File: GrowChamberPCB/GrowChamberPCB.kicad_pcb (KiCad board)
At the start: 2 copper layers, 100 x 100 mm, 194 parts, among them J1 Mister, J10 FoggerBasin, J11 TP, J12 Moisture Sensor 3, J13 Moisture Sensor 2, J14 UART, J15 FAE Fan, J16 DrainLevel, J17 TP, J18 TP, J19 TP, J2 Moisture Sensor 1, J20 TP, J21 TP, J22 TP, J23 TP, J24 TP, J25 TP, J26 TP, J27 TP, J28 TP, J29 TP, J3 SCD30, J30 TP, J31 TP, J32 TP, J33 TP, J34 TP, J35 TP, J36 TP, J37 TP, J38 TP, J39 TP, J4 Heater Fans, J40 TP, J41 TP, J42 TP, J43 TP, J44 TP, J45 TP, J47 Conn_01x04, J48 Conn_01x09, J49 TP, J5 Fogger Solenoid, J50 TP, J51 TP, J52 TP, J53 TP, J6 Drain Solenoid, J7 Water Solenoid, J8 Glycol Solenoid, J9 CircFan, P1 12V_In, P2 120V, P3 Screw Terminal, Q1 MOSFET, Q10 NPN, Q11 MOSFET, Q12 NPN, Q13 MOSFET, Q15 NPN, Q17 NPN, Q18 MOSFET, Q2 NPN, Q3 MOSFET, Q4 NPN, Q5 MOSFET, Q6 NPN, Q7 MOSFET, Q8 BRT30N70P3, Q9 NPN, SW1 Reset_Button_Internal, SW2 ResetButton_External, SW3 Bootmode_Internal, SW4 BootMode_External, U10 1N4007W, U11 AP63203WU-7, U12 1N4007W, U13 1N4007W, U14 1N4007W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

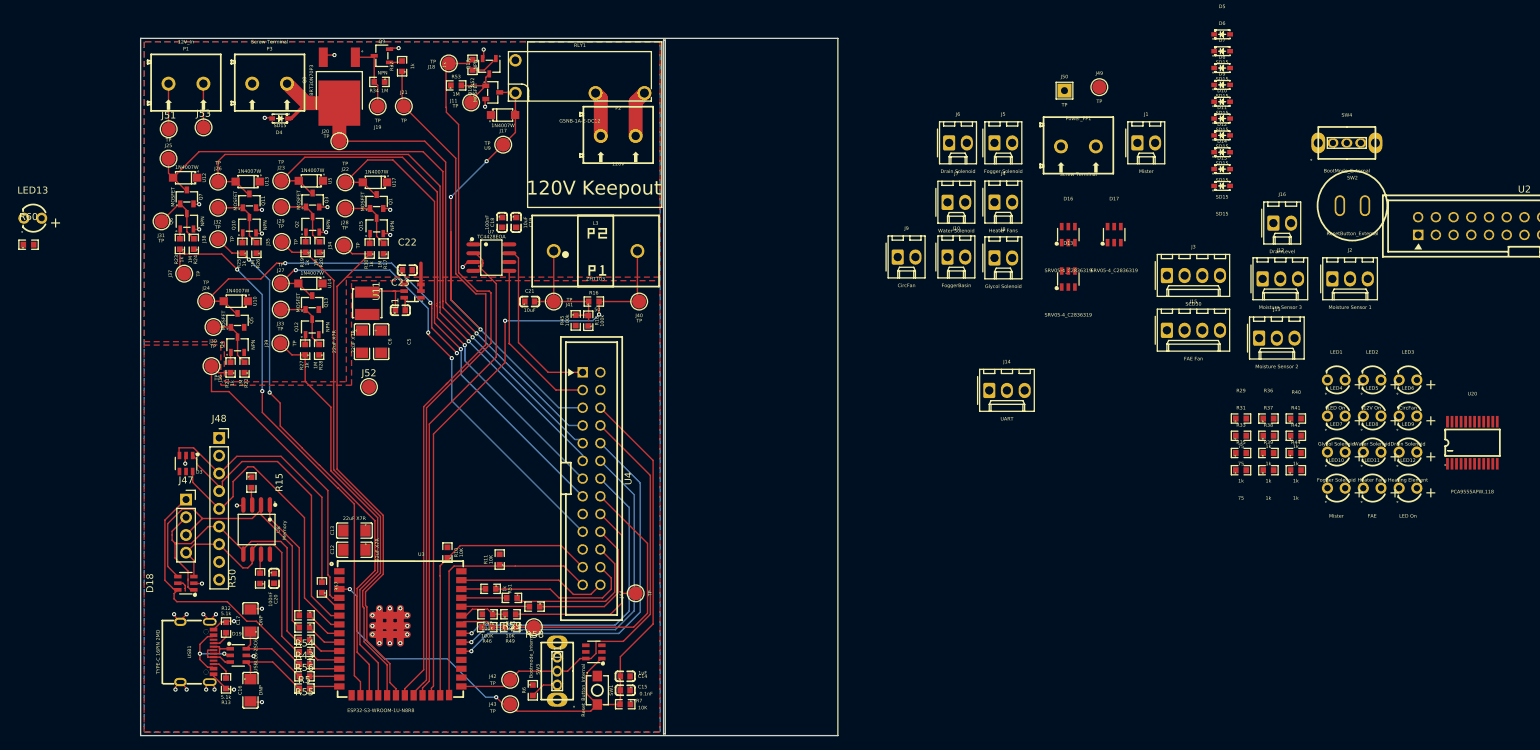
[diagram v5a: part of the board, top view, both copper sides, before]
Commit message: made a 4 layer board instead of 2
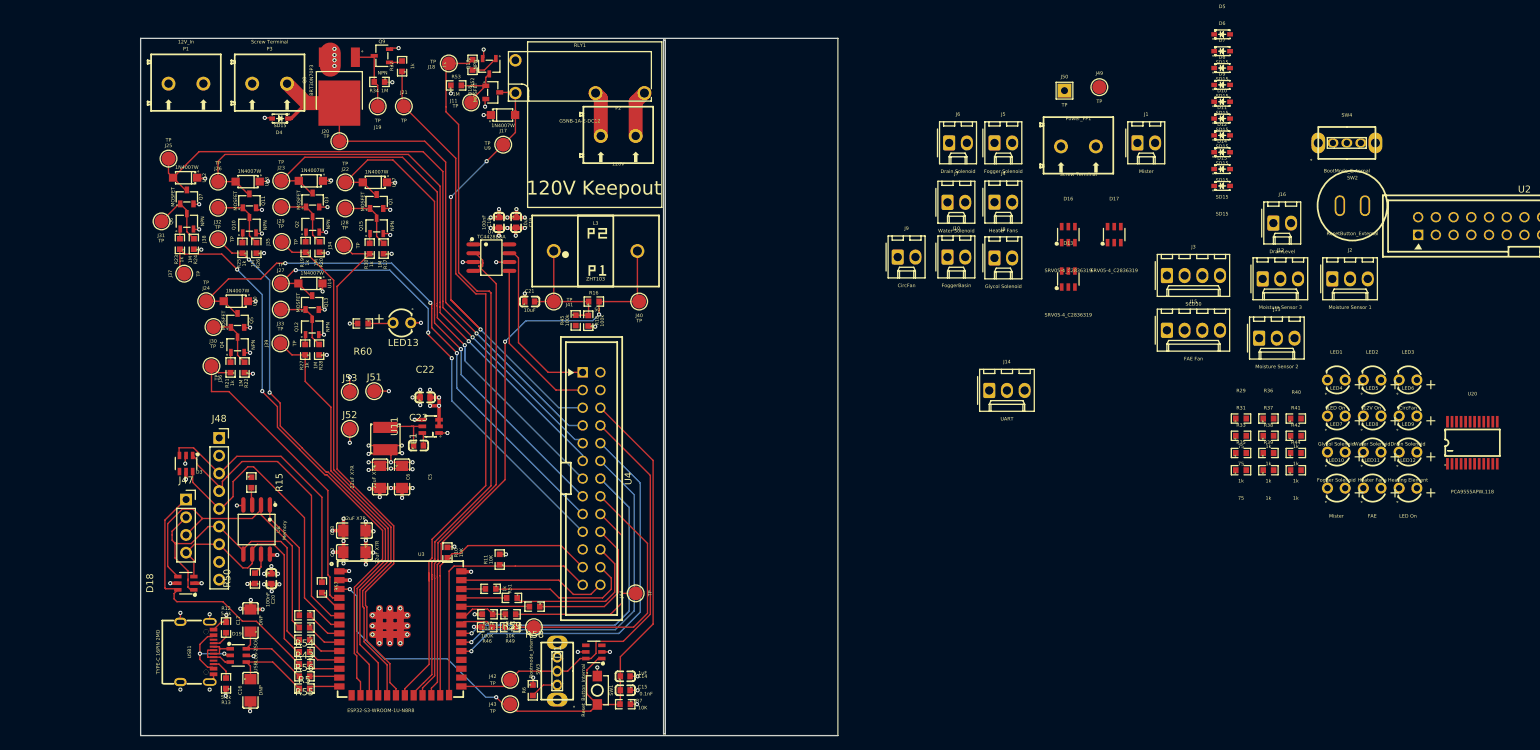
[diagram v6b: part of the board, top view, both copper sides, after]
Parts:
- moved LED13 55.0 mm to (49.5, 52.8), turned to 180 degrees
- moved R60 49.3 mm to (43.9, 52.9), turned to 180 degrees
- moved J51 47.8 mm to (45.5, 62.6)
- moved J53 43.3 mm to (42.0, 62.7)
- moved C5 19.6 mm to (49.5, 74.9)
- moved C23 19.6 mm to (51.9, 70.4)
- moved C6 19.6 mm to (46.4, 74.9)
- moved L1 19.6 mm to (47.1, 69.4)
- moved U11 19.6 mm to (53.6, 67.7)
- moved C22 18.4 mm to (52.8, 63.5)
- moved J52 6.60 mm to (42.0, 68.0)
- moved R50 0.74 mm to (28.4, 89.4)
- moved C18 0.45 mm to (63.4, 38.4)
- moved C20 0.39 mm to (30.8, 89.5)
- moved C12 0.35 mm to (42.7, 85.7)
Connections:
- LED13 pad 1: GND_FP -> GND
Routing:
- net 3.3V: track 1.99 -> 49.9 mm, vias 0 -> 31
- net 12V: track 10.5 -> 44.0 mm, vias 0 -> 27
- net GND: track 79.5 -> 110.6 mm, vias 42 -> 80
- net DrainSol: track 50.9 -> 81.4 mm
- net Heater_ON: track 77.0 -> 67.2 mm
- net Net-(LED13-A): track 0.00 -> 3.62 mm
- net WaterSol_IO: track 81.6 -> 85.1 mm
- net KSD_Fault: track 86.9 -> 85.2 mm
- net GlycolSol_IO: track 77.4 -> 78.8 mm
- net HeaterFans_IO: track 75.2 -> 76.5 mm
- net CircFan_IO: track 59.5 -> 60.7 mm
- net FoggerSol_IO: track 74.6 -> 75.8 mm
- net Net-(J41-Pin_1): track 19.6 -> 18.8 mm
- net CS_SD: track 39.2 -> 39.8 mm
- added copper zone on In2.Cu, net 12V
- added copper zone on In2.Cu, net 3.3V
- added copper zone on In1.Cu, net GND
- removed copper zone on F.Cu, net 12V
- removed copper zone on F.Cu, net 3.3V
- removed copper zone on B.Cu, net GND
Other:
- copper layers 2 -> 4
- rule pad_to_mask_clearance: 0 -> 0.1

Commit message: fillin stuff out
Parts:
- moved U2 105.4 mm to (105.1, 34.6), turned to 90 degrees
- moved J2 95.5 mm to (92.3, 16.4)
- moved SW2 95.1 mm to (93.6, 59.2)
- moved SW4 93.6 mm to (94.2, 49.6)
- moved J16 87.9 mm to (92.4, 70.0)
- moved Power_FP1 87.9 mm to (105.8, 105.4)
- moved J13 85.7 mm to (92.3, 24.8)
- moved J12 81.7 mm to (92.3, 33.4)
- moved J1 80.6 mm to (92.5, 78.0)
- moved J5 73.0 mm to (92.9, 87.0)
- moved J3 68.7 mm to (90.6, 42.2)
- moved J6 66.4 mm to (100.0, 87.2)
- moved J15 64.4 mm to (99.5, 78.0)
- moved J7 63.2 mm to (106.8, 95.2)
- moved J8 62.1 mm to (100.0, 95.2)
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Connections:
- J12 pad 3: GPIO4_FP -> SoilMoisture4_FP
- J13 pad 3: GPIO2_FP -> SoilMoisture2_FP
- J2 pad 3: GPIO1_FP -> SoilMoisture1_FP
- U2 pad 1: unconnected-(U2-Pad1) -> Piezo2_FP
- U2 pad 10: unconnected-(U2-Pad10) -> SoilMoisture4_FP
- U2 pad 11: unconnected-(U2-Pad11) -> GlycolSol_FP
- U2 pad 12: unconnected-(U2-Pad12) -> SoilMoisture2_FP
- U2 pad 13: unconnected-(U2-Pad13) -> FoggerSol_FP
- U2 pad 14: unconnected-(U2-Pad14) -> SoilMoisture1_FP
- U2 pad 15: unconnected-(U2-Pad15) -> Heater Fans_FP
- U2 pad 16: unconnected-(U2-Pad16) -> Drain_Level_FP
- U2 pad 17: unconnected-(U2-Pad17) -> DrainSol_FP
- U2 pad 18: unconnected-(U2-Pad18) -> Fogger_Basin_Float_Switch_FP
- U2 pad 19: unconnected-(U2-Pad19) -> Circ_Fan_FP
- U2 pad 2: unconnected-(U2-Pad2) -> 3.3V_FP
- U2 pad 20: unconnected-(U2-Pad20) -> RXD0_FP
- U2 pad 22: unconnected-(U2-Pad22) -> TXD0_FP
- U2 pad 23: unconnected-(U2-Pad23) -> SDA_FP
- U2 pad 24: unconnected-(U2-Pad24) -> External_Fan_PWM_FP
- U2 pad 25: unconnected-(U2-Pad25) -> SCL_FP
- U2 pad 26: unconnected-(U2-Pad26) -> Fan_Tach_FP
- U2 pad 3: unconnected-(U2-Pad3) -> Piezo1_FP
- U2 pad 4: unconnected-(U2-Pad4) -> 3.3V_FP
- U2 pad 5: unconnected-(U2-Pad5) -> Heater_ON_FP
- U2 pad 6: unconnected-(U2-Pad6) -> EN_FP
- U2 pad 7: unconnected-(U2-Pad7) -> LEDs_FP
- U2 pad 8: unconnected-(U2-Pad8) -> BootMode_FP
- U2 pad 9: unconnected-(U2-Pad9) -> WaterSol_FP
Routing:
- net GND: track 110.6 -> 112.3 mm, vias 80 -> 81
- net KSD_Fault: track 85.2 -> 86.4 mm
- net 3.3V: track 49.9 -> 50.8 mm, vias 31 -> 32
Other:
- outline, holes or cut-outs redrawn

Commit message: finished routing
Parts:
- removed C18, C23: 100nF, easyeda2kicad:C0603
- removed C19, C21, C22: 10uF, easyeda2kicad:C0603
- removed D13, D16, D17, D18: SRV05-4_C2836319, easyeda2kicad:SOT-23-6_L2.9-W1.6-P0.95-LS2.8-BL
- removed D14, D15: SD15, easyeda2kicad:SOD-323_L1.7-W1.3-LS2.6-RD
- removed D19: USBLC6-2SC6, easyeda2kicad:SOT-23-6_L2.9-W1.6-P0.95-LS2.8-BL
- removed J11, J17, J18, J19, J20, J21, J22, J23, J24, J25, J26, J27, J28, J29, J30, J31, J32, J33: TP, TestPoint:TestPoint_Pad_D2.0mm
- removed L1: ANR4030T3R9M, easyeda2kicad:IND-SMD_L4.0-W4.0
- removed LED11: FAE, easyeda2kicad:LED-TH_BD3.9-P2.54-RD_RED
- removed LED12: LED On, easyeda2kicad:LED-TH_BD3.9-P2.54-RD_RED
- removed Q1, Q18, Q3, Q5: MOSFET, easyeda2kicad:SOT-23-3_L2.9-W1.3-P1.90-LS2.4-BR
- removed Q17, Q2, Q4, Q6, Q9: NPN, easyeda2kicad:SOT-23-3_L3.0-W1.7-P0.95-LS2.9-BR
- removed Q8: BRT30N70P3, easyeda2kicad:TO-252-2_L6.6-W6.1-P4.60-LS10.0-BR-CW
- removed R40, R41, R42, R44, R51, R52: 1k, easyeda2kicad:R0603
- removed R48, R49, R50: 10K, easyeda2kicad:R0603
- removed R53: 1M, easyeda2kicad:R0603
- removed R54, R55, R56, R57, R58, R59: 33, easyeda2kicad:R0603
- removed SW2: ResetButton_External, easyeda2kicad:CONN-TH_PB-05B-R
- removed U10, U5, U9: 1N4007W, easyeda2kicad:SOD-123FL_L2.7-W1.8-LS3.7-RD
- removed U20: PCA9555APW,118, easyeda2kicad:TSSOP-24_L7.8-W4.4-P0.65-LS6.4-BL
- added C1: 4.7uF - X7R, easyeda2kicad:C1206, F.Cu at (106.8, 80.3)
- added C10: 22uF - X5R, easyeda2kicad:C1206, F.Cu at (93.6, 108.9)
- added C11: 47uF X5R, easyeda2kicad:C1206, F.Cu at (100.3, 92.7)
- added C2: 10nF, easyeda2kicad:C0603, F.Cu at (102.7, 85.2)
- added C3: 47uF X5R, easyeda2kicad:C1206, F.Cu at (95.1, 92.7)
- added C4: 100nF, easyeda2kicad:C0402, F.Cu at (102.9, 90.9)
- added C7: 150pF, easyeda2kicad:C0603, F.Cu at (108.8, 91.3)
- added C8: 1500pF, easyeda2kicad:C0603, F.Cu at (104.7, 91.2)
- added C9: 47uF X5R, easyeda2kicad:C1206, F.Cu at (97.7, 92.7)
- added D2: SS34, easyeda2kicad:SMA_L4.3-W2.6-LS5.2-RD, F.Cu at (100.4, 79.5)
- added D20: 1N4007W, easyeda2kicad:SOD-123FL_L2.7-W1.8-LS3.8-RD, F.Cu at (106.0, 61.8)
- added D27: 1n4007W, easyeda2kicad:SOD-123FL_L2.7-W1.8-LS3.8-RD, F.Cu at (82.4, 64.5)
- added D28: 1n4007W, easyeda2kicad:SOD-123FL_L2.7-W1.8-LS3.8-RD, F.Cu at (82.4, 51.8)
- added D29: 1n4007W, easyeda2kicad:SOD-123FL_L2.7-W1.8-LS3.8-RD, F.Cu at (73.6, 60.4)
- added D30: 1n4007W, easyeda2kicad:SOD-123FL_L2.7-W1.8-LS3.8-RD, F.Cu at (73.6, 73.1)
- added D31: 1n4007W, easyeda2kicad:SOD-123FL_L2.7-W1.8-LS3.8-RD, F.Cu at (82.4, 77.6)
- added D32: 1n4007W, easyeda2kicad:SOD-123FL_L2.7-W1.8-LS3.8-RD, F.Cu at (73.6, 47.6)
- added D33: 1n4007W, easyeda2kicad:SOD-123FL_L2.7-W1.8-LS3.8-RD, F.Cu at (81.7, 39.5)
- added D34: 1n4007W, easyeda2kicad:SOD-123FL_L2.7-W1.8-LS3.8-RD, F.Cu at (92.1, 49.2)
- added H1: MountingHole, MountingHole:MountingHole_3.2mm_M3_Pad_Via, F.Cu at (131.4, 131.0)
- added H2: MountingHole, MountingHole:MountingHole_3.2mm_M3_Pad_Via, F.Cu at (131.4, 41.0)
- added H3: MountingHole, MountingHole:MountingHole_3.2mm_M3_Pad_Via, F.Cu at (74.7, 131.0)
- added H4: MountingHole, MountingHole:MountingHole_3.2mm_M3_Pad_Via, F.Cu at (74.7, 41.0)
- added H5: MountingHole, MountingHole:MountingHole_3.2mm_M3_Pad_Via, F.Cu at (153.2, 41.0)
- added H6: MountingHole, MountingHole:MountingHole_3.2mm_M3_Pad_Via, F.Cu at (153.2, 131.0)
- added J46: TP, TestPoint:TestPoint_Pad_D2.0mm, F.Cu at (77.7, 79.0)
- added J54: TP, TestPoint:TestPoint_Pad_D2.0mm, F.Cu at (77.7, 53.5)
- added J55: TP, TestPoint:TestPoint_Pad_D2.0mm, F.Cu at (77.7, 47.8)
- added J56: TP, TestPoint:TestPoint_Pad_D2.0mm, F.Cu at (85.1, 44.9)
- added J57: TP, TestPoint:TestPoint_Pad_D2.0mm, F.Cu at (85.9, 39.5)
- added J58: TP, TestPoint:TestPoint_Pad_D2.0mm, F.Cu at (96.2, 55.1)
- added J59: TP, TestPoint:TestPoint_Pad_D2.0mm, F.Cu at (96.2, 49.4)
- added J60: TP, TestPoint:TestPoint_Pad_D2.0mm, F.Cu at (148.2, 39.0)
- added L2: SL0650-150M, easyeda2kicad:IND-SMD_L7.0-W6.6, F.Cu at (98.2, 85.4)
- added Q14: AO3400A, easyeda2kicad:SOT-23-3_L2.9-W1.3-P1.90-LS2.4-BR, F.Cu at (73.6, 50.6)
- added Q16: AO3400A, easyeda2kicad:SOT-23-3_L2.9-W1.3-P1.90-LS2.4-BR, F.Cu at (92.1, 52.2)
- added R1: 10k, easyeda2kicad:R0603, F.Cu at (110.6, 91.4)
- added R14: 10k, easyeda2kicad:R0603, F.Cu at (115.3, 121.4)
- added R2: 5k6, easyeda2kicad:R0603, F.Cu at (106.7, 92.0)
- added R3: 300, easyeda2kicad:R0603, F.Cu at (106.7, 95.1)
- added R4: 560, easyeda2kicad:R0603, F.Cu at (102.9, 93.5)
- added R61: 10k, easyeda2kicad:R0603, F.Cu at (83.4, 71.1)
- added R62: 1k, easyeda2kicad:R0603, F.Cu at (81.4, 58.4)
- added R63: 10k, easyeda2kicad:R0603, F.Cu at (83.4, 58.4)
- added R64: 1k, easyeda2kicad:R0603, F.Cu at (72.6, 67.0)
- added R65: 10k, easyeda2kicad:R0603, F.Cu at (74.6, 67.0)
- added R66: 1k, easyeda2kicad:R0603, F.Cu at (72.6, 79.7)
- added R67: 10k, easyeda2kicad:R0603, F.Cu at (74.6, 79.7)
- added R68: 1k, easyeda2kicad:R0603, F.Cu at (81.4, 84.2)
- added R69: 10k, easyeda2kicad:R0603, F.Cu at (83.4, 84.2)
- added R70: 1k, easyeda2kicad:R0603, F.Cu at (72.6, 54.2)
- added R71: 10k, easyeda2kicad:R0603, F.Cu at (74.6, 54.2)
- added R72: 1k, easyeda2kicad:R0603, F.Cu at (80.9, 45.7)
- added R73: 10k, easyeda2kicad:R0603, F.Cu at (82.7, 45.7)
- added R74: 1k, easyeda2kicad:R0603, F.Cu at (91.2, 55.8)
- added R75: 10k, easyeda2kicad:R0603, F.Cu at (93.2, 55.8)
- added SW5: On/Off, easyeda2kicad:SW-TH_SS-12D02-VG4, F.Cu at (161.4, 100.7)
- added U15: SRV05-4A, easyeda2kicad:SOT-23-6_L2.9-W1.6-P0.95-LS2.9-BL, F.Cu at (150.4, 70.0)
- added U16: SRV05-4A, easyeda2kicad:SOT-23-6_L2.9-W1.6-P0.95-LS2.9-BL, F.Cu at (80.9, 118.6)
- added U18: SRV05-4A, easyeda2kicad:SOT-23-6_L2.9-W1.6-P0.95-LS2.9-BL, F.Cu at (79.3, 100.3)
- added U6: TPS5430DDAR, easyeda2kicad:ESOP-8_L4.9-W3.9-P1.27-LS6.0-TL-EP, F.Cu at (106.4, 85.3)
- C12, C6: value 22uF X7R -> 10uF; footprint easyeda2kicad:C1206 -> easyeda2kicad:C0805
- C13: value 22uF X7R -> 4.7uF - X7R
- C14: value 1uF -> 150pF
- C15: value 0.1nF -> 100nF; footprint easyeda2kicad:C0603 -> easyeda2kicad:C0402
- C5: value 22uF X7R -> 100nF; footprint easyeda2kicad:C1206 -> easyeda2kicad:C0402
- D1, D3: value SRV05-4_C2836319 -> SMF15A; footprint easyeda2kicad:SOT-23-6_L2.9-W1.6-P0.95-LS2.8-BL -> easyeda2kicad:SOD-123FL_L2.7-W1.8-LS3.8-RD
- D10, D11, D12, D5, D6, D7, D8, D9: value SD15 -> SMF15A; footprint easyeda2kicad:SOD-323_L1.7-W1.3-LS2.6-RD -> easyeda2kicad:SOD-123FL_L2.7-W1.8-LS3.8-RD
- J49: value TP -> 12V
- J50: value TP -> Gnd
- LED10: value Mister -> 12V On
- LED4: value Glycol Solenoid -> 12V On
- LED5: value Water Solenoid -> 12V On
- LED6: value Drain Solenoid -> 12V On
- LED7: value Fogger Solenoid -> 12V On
- P3: value Screw Terminal -> LED Connector
- Q10, Q12, Q15: value NPN -> AO3400A; footprint easyeda2kicad:SOT-23-3_L3.0-W1.7-P0.95-LS2.9-BR -> easyeda2kicad:SOT-23-3_L2.9-W1.3-P1.90-LS2.4-BR
- Q11, Q13, Q7: value MOSFET -> AO3400A
- R10: value 10K -> 1k
- R11, R15, R7: value 10K -> 33
- R12, R13: value 5.1k -> 33
- R16: value 50 -> 1k
- R17, R24, R26, R28: value 1M -> 10k
- R18: value 100k -> 1k
- R19: value 1k -> 100k
- R20: value 1M -> 100k
- R22: value 1M -> 5.1k
- R23: value 1k -> 5.1k
- R25, R27, R30: value 1k -> 10k
- R29: value 75 -> 33
- R31: value 75 -> 10k
- R34: value 1M -> 1k
- R35: value 75 -> 1k
- R36: value 1k -> 0603WAF750JT5E
- R46: value 100K -> 33
- R47: value 100K -> 100k
- R5: value 33 -> 50
- R6: value 10K -> 22
- R9: value 22 -> 33
- SW1: value Reset_Button_Internal -> TS-1088-AR02016; footprint easyeda2kicad:SW-SMD_L4.0-W2.9-LS5.0 -> easyeda2kicad:SW-SMD_L3.9-W3.0-P4.45
- U11: value AP63203WU-7 -> SRV05-4A; footprint easyeda2kicad:TSOT-26_L2.9-W1.6-P0.95-LS2.8-BL -> easyeda2kicad:SOT-23-6_L2.9-W1.6-P0.95-LS2.9-BL
- U12, U13, U14, U17: value 1N4007W -> SRV05-4A; footprint easyeda2kicad:SOD-123FL_L2.7-W1.8-LS3.7-RD -> easyeda2kicad:SOT-23-6_L2.9-W1.6-P0.95-LS2.9-BL
- U2: value ZX-IDC2.54-2-13PZZ -> 2x13
- moved U12 156.7 mm to (161.4, 96.0), turned to 0 degrees
- moved R32 152.2 mm to (164.8, 115.4), turned to 180 degrees
- moved D3 139.7 mm to (147.0, 127.8), turned to 90 degrees
- moved R34 137.3 mm to (150.6, 107.5), turned to 0 degrees
- moved R24 131.3 mm to (114.7, 132.0)
- moved P1 127.0 mm to (130.4, 78.6), turned to 90 degrees
- moved U13 126.2 mm to (150.6, 59.5), turned to 90 degrees
- moved U17 120.7 mm to (122.5, 125.7)
- moved R19 114.8 mm to (118.5, 121.4), turned to 180 degrees
- moved R20 111.8 mm to (118.5, 119.1), turned to 180 degrees
- moved J49 108.7 mm to (157.0, 127.4), turned to 180 degrees
- moved R18 105.8 mm to (154.0, 124.2), turned to -90 degrees
- moved J50 105.4 mm to (156.8, 124.2), turned to -90 degrees
- moved R17 103.0 mm to (115.3, 119.1), turned to 180 degrees
- moved R23 102.2 mm to (79.3, 123.0), turned to -90 degrees
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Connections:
- C12 pad 2: 3.3V -> Net-(J41-Pin_1)
- C13 pad 2: 3.3V -> EN
- C15 pad 1: GND -> 3.3V
- C15 pad 2: EN -> GND
- C16 pad 1: Out_D+ -> D+
- C17 pad 1: Out_D- -> D-
- C5 pad 1: 3.3V -> GND
- C5 pad 2: GND -> 12V
- C6 pad 1: 3.3V -> GND
- C6 pad 2: GND -> 12V
- D1 pad 1: EN -> External_Fan_PWM_FP
- D1 pad 2: GND -> GND_FP
- D10 pad 1: WaterSol_FP -> DrainSol_FP
- D11 pad 1: GlycolSol_FP -> FoggerSol_FP
- D12 pad 1: Piezo1_FP -> GlycolSol_FP
- D3 pad 1: Display_Reset -> Fan_Tach_FP
- D3 pad 2: GND -> GND_FP
- D7 pad 1: Heater Fans_FP -> Piezo1_FP
- D8 pad 1: FoggerSol_FP -> Heater Fans_FP
- D9 pad 1: DrainSol_FP -> WaterSol_FP
- J1 pad 1: Piezo1_FP -> Piezo2_FP
- J1 pad 2: Piezo2_FP -> Piezo1_FP
- J16 pad 1: 3.3V_FP -> Drain_Level_FP
- J16 pad 2: Drain_Level_FP -> 3.3V_FP
- J34 pad 1: HeaterFans_IO -> Net-(J34-Pin_1)
- J35 pad 1: FoggerSol_IO -> GlycolSol
- J36 pad 1: DrainSolIO -> Net-(J36-Pin_1)
- J37 pad 1: WaterSol_IO -> WaterSol
- J38 pad 1: GlycolSol_IO -> Net-(J38-Pin_1)
- J39 pad 1: CircFan_IO -> Heater Fans
- J47 pad 3: MISO -> MISO_ESD
- J5 pad 1: FoggerSol_FP -> WaterSol_FP
- J51 pad 1: GND -> Circ_Fan
- J52 pad 1: 3.3V -> Net-(J52-Pin_1)
- J53 pad 1: 12V -> DrainSol
- J7 pad 1: WaterSol_FP -> FoggerSol_FP
- LED10 pad 1: Net-(LED10-K) -> GlycolSol_FP
- LED4 pad 1: GlycolSol_FP -> FoggerSol_FP
- LED5 pad 1: WaterSol_FP -> DrainSol_FP
- LED6 pad 1: DrainSol_FP -> WaterSol_FP
- LED7 pad 1: FoggerSol_FP -> Net-(LED7-K)
- LED7 pad 2: Net-(LED7-A) -> Heartbeat_LED_FP
- Q10 pad 1: Net-(Q10-B) -> Net-(J36-Pin_1)
- Q10 pad 3: Net-(J32-Pin_1) -> WaterSol
- Q11 pad 1: Net-(J32-Pin_1) -> Net-(J38-Pin_1)
- Q11 pad 3: GlycolSol -> Heater Fans
- Q12 pad 1: Net-(Q12-B) -> Net-(J46-Pin_1)
- Q12 pad 3: Net-(J33-Pin_1) -> Circ_Fan
- Q13 pad 1: Net-(J33-Pin_1) -> Net-(J52-Pin_1)
- Q13 pad 3: Circ_Fan -> DrainSol
- Q15 pad 1: Net-(Q15-B) -> Net-(J56-Pin_1)
- Q15 pad 3: Net-(J28-Pin_1) -> LEDs
- Q7 pad 1: Net-(J31-Pin_1) -> Net-(J34-Pin_1)
- Q7 pad 3: WaterSol -> GlycolSol
- R10 pad 1: SDA -> Net-(U3-IO1)
- R10 pad 2: 3.3V -> External_Fan_PWM
- R11 pad 1: SCL -> CS_SD
- R11 pad 2: 3.3V -> Net-(U3-IO16)
- R12 pad 1: GND -> SCK
- R12 pad 2: Net-(USB1-CC1) -> Net-(U3-IO5)
- R13 pad 1: GND -> MOSI
- R13 pad 2: Net-(USB1-CC2) -> Net-(U3-IO6)
- R15 pad 1: 3.3V -> Net-(U8-DO)
- R15 pad 2: Net-(U8-IO2) -> MISO
- R16 pad 1: Net-(J41-Pin_1) -> Net-(LED1-A)
- R16 pad 2: KSD_Fault -> 12V_FP
- R17 pad 1: 12V -> Fogger_Basin_Float_Switch
- R17 pad 2: Net-(J28-Pin_1) -> FloatSwitch_IO
- R18 pad 1: 3.3V -> Net-(LED2-A)
- R18 pad 2: Net-(J41-Pin_1) -> 12V_FP
- R19 pad 1: FoggerSol_IO -> GND
- R19 pad 2: Net-(Q2-B) -> DrainLevel_IO
- R20 pad 1: 12V -> GND
- R20 pad 2: Net-(J29-Pin_1) -> FloatSwitch_IO
- R21 pad 1: DrainSolIO -> Net-(LED13-A)
- R21 pad 2: Net-(Q4-B) -> 12V
- R22 pad 1: 12V -> Net-(USB1-CC1)
- R22 pad 2: Net-(J30-Pin_1) -> GND
- R23 pad 1: WaterSol_IO -> Net-(USB1-CC2)
- R23 pad 2: Net-(Q6-B) -> GND
- R24 pad 1: 12V -> 3.3V
- R24 pad 2: Net-(J31-Pin_1) -> Net-(R24-Pad2)
- R25 pad 1: GlycolSol_IO -> 3.3V
- R25 pad 2: Net-(Q10-B) -> EN
- R26 pad 1: 12V -> Net-(U8-IO3)
- R26 pad 2: Net-(J32-Pin_1) -> 3.3V
- R27 pad 1: CircFan_IO -> 3.3V
- R27 pad 2: Net-(Q12-B) -> Net-(U8-IO2)
- R28 pad 1: 12V -> SCL
- R28 pad 2: Net-(J33-Pin_1) -> 3.3V
- R29 pad 1: Net-(LED10-A) -> MISO_ESD
- R29 pad 2: 3.3V_FP -> MISO
- R30 pad 1: HeaterFans_IO -> SDA
- R30 pad 2: Net-(Q15-B) -> 3.3V
- R31 pad 1: Net-(LED12-A) -> 3.3V
- R31 pad 2: 3.3V_FP -> Net-(R31-Pad2)
- R32 pad 1: LEDIO -> Net-(LED3-A)
- R32 pad 2: Net-(Q9-B) -> 12V_FP
- R33 pad 1: Net-(LED3-A) -> Net-(LED4-A)
- R34 pad 1: 12V -> Net-(LED5-A)
- R34 pad 2: Net-(J19-Pin_1) -> 12V_FP
- R35 pad 1: Net-(LED11-A) -> Net-(LED6-A)
- R35 pad 2: 3.3V_FP -> 12V_FP
- R36 pad 1: Net-(LED4-A) -> Net-(LED7-K)
- R36 pad 2: 12V_FP -> GND_FP
- R37 pad 1: Net-(LED5-A) -> Net-(LED10-A)
- R38 pad 1: Net-(LED6-A) -> Net-(LED8-A)
- R39 pad 1: Net-(LED7-A) -> Net-(LED9-A)
- R43 pad 1: Net-(U3-IO16) -> CS_Memory
- R43 pad 2: MISO -> Net-(U3-IO15)
- R45 pad 1: Net-(J41-Pin_1) -> GND
- R45 pad 2: GND -> Net-(J41-Pin_1)
- R46 pad 1: DrainLevel_IO -> CS_Display
- R46 pad 2: GND -> Net-(U3-IO8)
- R47 pad 1: FloatSwitch_IO -> Net-(J41-Pin_1)
- R47 pad 2: GND -> 3.3V
- R5 pad 1: Net-(U3-IO18) -> Net-(J41-Pin_1)
- R5 pad 2: SCK -> KSD_Fault
- R6 pad 1: 3.3V -> D-
- R6 pad 2: Net-(R6-Pad2) -> IO19
- R60 pad 1: Net-(LED13-A) -> GlycolSol_IO
- R60 pad 2: 12V -> Net-(J34-Pin_1)
- R7 pad 1: 3.3V -> Net-(U3-RXD0)
- R7 pad 2: EN -> RXD0
- R8 pad 1: Out_D- -> D+
- R8 pad 2: IO19 -> IO20
- R9 pad 1: Out_D+ -> Net-(U3-TXD0)
- R9 pad 2: IO20 -> TXD0
- SW3 pad 1: Net-(R6-Pad2) -> Net-(R24-Pad2)
- SW4 pad 1: unconnected-(SW4-Pad1) -> Net-(R31-Pad2)
- U11 pad 1: 3.3V -> SoilMoisture4_FP
- U11 pad 2: 12V -> GND_FP
- U11 pad 3: 12V -> SoilMoisture2_FP
- U11 pad 4: GND -> SoilMoisture1_FP
- U11 pad 5: Net-(U11-SW) -> 3.3V_FP
- U11 pad 6: Net-(U11-BST) -> /Faceplate/3.3V ESD/IO3
- U12 pad 1: 12V -> /Faceplate/Data Line ESD/IO1
- U12 pad 2: WaterSol -> GND_FP
- U13 pad 1: 12V -> TXD0_FP
- U13 pad 2: GlycolSol -> GND_FP
- U14 pad 1: 12V -> CS_SD
- U14 pad 2: Circ_Fan -> GND_FP
- U17 pad 1: 12V -> /ESP32/Data Line ESD3/IO1
- U17 pad 2: Heater Fans -> GND_FP
- U2 pad 1: Piezo2_FP -> Heater_ON_FP
- U2 pad 10: SoilMoisture4_FP -> RXD0_FP
- U2 pad 11: GlycolSol_FP -> SCL_FP
- U2 pad 12: SoilMoisture2_FP -> SDA_FP
- U2 pad 13: FoggerSol_FP -> SoilMoisture4_FP
- U2 pad 15: Heater Fans_FP -> SoilMoisture2_FP
- U2 pad 16: Drain_Level_FP -> WaterSol_FP
- U2 pad 17: DrainSol_FP -> GlycolSol_FP
- U2 pad 18: Fogger_Basin_Float_Switch_FP -> 3.3V_FP
- U2 pad 19: Circ_Fan_FP -> DrainSol_FP
- U2 pad 2: 3.3V_FP -> EN_FP
- U2 pad 20: RXD0_FP -> 3.3V_FP
- U2 pad 21: unconnected-(U2-Pad21) -> FoggerSol_FP
- U2 pad 22: TXD0_FP -> Heater Fans_FP
- U2 pad 23: SDA_FP -> Fan_Tach_FP
- U2 pad 24: External_Fan_PWM_FP -> Circ_Fan_FP
- U2 pad 25: SCL_FP -> External_Fan_PWM_FP
- U2 pad 26: Fan_Tach_FP -> Heartbeat_LED_FP
- U2 pad 3: Piezo1_FP -> LEDs_FP
- U2 pad 4: 3.3V_FP -> Fogger_Basin_Float_Switch_FP
- U2 pad 5: Heater_ON_FP -> Piezo2_FP
- U2 pad 6: EN_FP -> Drain_Level_FP
- U2 pad 7: LEDs_FP -> Piezo1_FP
- U2 pad 9: WaterSol_FP -> TXD0_FP
- U3 pad 10: Net-(U3-IO17) -> DC_Display
- U3 pad 11: Net-(U3-IO18) -> Display_Reset
- U3 pad 15: unconnected-(U3-IO3-Pad15) -> Heartbeat_LED
- U3 pad 16: WaterSol_IO -> HeaterFans_IO
- U3 pad 17: GlycolSol_IO -> FoggerSol_IO
- U3 pad 18: CircFan_IO -> DrainSolIO
- U3 pad 19: FoggerSol_IO -> GlycolSol_IO
- U3 pad 20: HeaterFans_IO -> WaterSol_IO
- U3 pad 25: SDA -> Soil_Moisture2
- U3 pad 26: SCL -> Soil_Moisture1
- U3 pad 32: Soil_Moisture2 -> SCL
- U3 pad 33: Soil_Moisture1 -> SDA
- U3 pad 38: Net-(U3-IO2) -> Fan_Tach
- U3 pad 39: Fan_Tach -> Net-(U3-IO1)
- U3 pad 4: DrainSolIO -> CircFan_IO
- U3 pad 6: Display_Reset -> Net-(U3-IO6)
- U3 pad 7: DC_Display -> MISO
- U4 pad 1: Piezo2 -> Heater_ON
- U4 pad 10: Soil_Moisture4 -> RXD0
- U4 pad 11: GlycolSol -> SCL
- U4 pad 12: Soil_Moisture2 -> SDA
- U4 pad 13: FoggerSol -> Soil_Moisture4
- U4 pad 15: Heater Fans -> Soil_Moisture2
- U4 pad 16: Drain_Level -> WaterSol
- U4 pad 17: DrainSol -> GlycolSol
- U4 pad 18: Fogger_Basin_Float_Switch -> 3.3V
- U4 pad 19: Circ_Fan -> DrainSol
- U4 pad 2: 3.3V -> EN
- U4 pad 20: RXD0 -> 3.3V
- U4 pad 21: unconnected-(U4-Pad21) -> FoggerSol
- U4 pad 22: TXD0 -> Heater Fans
- U4 pad 23: SDA -> Fan_Tach
- U4 pad 24: External_Fan_PWM -> Circ_Fan
- U4 pad 25: SCL -> External_Fan_PWM
- U4 pad 26: Fan_Tach -> Heartbeat_LED
- U4 pad 3: Piezo1 -> LEDs
- U4 pad 4: 3.3V -> Fogger_Basin_Float_Switch
- U4 pad 5: Heater_ON -> Piezo2
- U4 pad 6: EN -> Drain_Level
- U4 pad 7: LEDs -> Piezo1
- U4 pad 9: WaterSol -> TXD0
- U8 pad 2: MISO -> Net-(U8-DO)
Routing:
- net GND: track 112.3 -> 0.00 mm, vias 81 -> 9
- net Fan_Tach_FP: track 0.00 -> 62.1 mm
- net External_Fan_PWM_FP: track 0.00 -> 61.6 mm
- net FoggerSol_FP: track 0.00 -> 56.9 mm
- net EN_FP: track 0.00 -> 55.0 mm, vias 0 -> 1
- net Heater Fans_FP: track 0.00 -> 51.9 mm, vias 0 -> 1
- net DrainSol_FP: track 0.00 -> 51.1 mm
- net 3.3V: track 50.8 -> 0.00 mm, vias 32 -> 0
- net WaterSol_FP: track 0.00 -> 50.2 mm
- net Circ_Fan_FP: track 0.00 -> 47.6 mm, vias 0 -> 1
- net BootMode_FP: track 0.00 -> 45.1 mm
- net 12V: track 44.0 -> 0.00 mm, vias 27 -> 0
- net DrainSol: track 81.4 -> 37.9 mm, vias 3 -> 1
- net SoilMoisture1_FP: track 0.00 -> 42.9 mm
- net GlycolSol_FP: track 0.00 -> 39.0 mm
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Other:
- board text added: "1K"
- board text added: "3.3V"
- board text added: "33"
- board text added: "47uF X5R x3"
- board text added: "Conn_01x0"
- board text added: "Heartbeat"
- board text added: "J39"
- board text added: "TS-1088-AR02016"
- board text removed: "120V Keepout"
